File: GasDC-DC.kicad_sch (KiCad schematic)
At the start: 18 parts, among them IC1 TPS56637RPAR, J1 Conn_01x02, Q1 2N7002_SOT-23-3

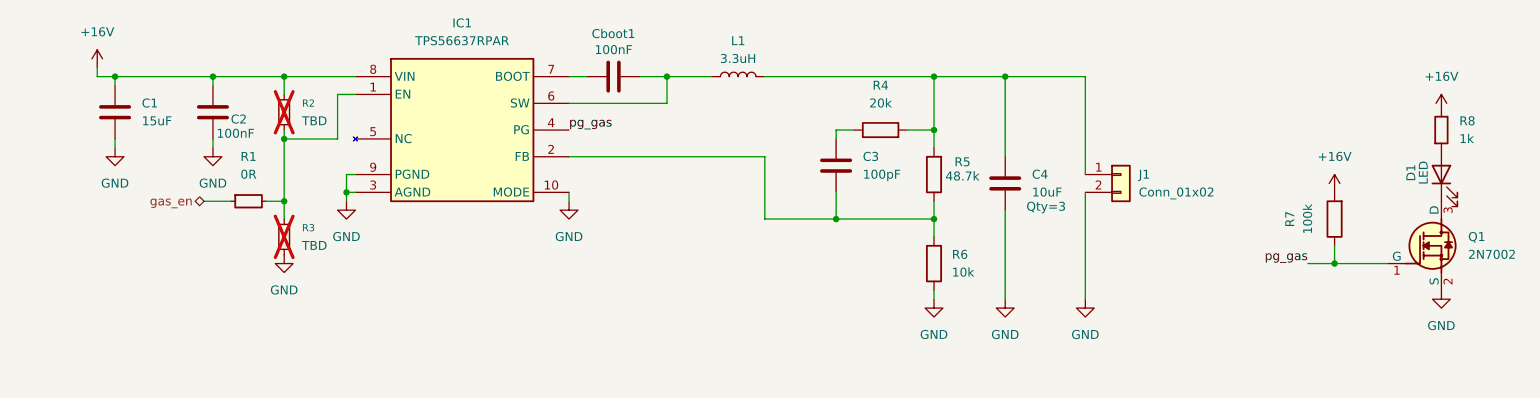
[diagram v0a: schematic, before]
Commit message: Minimal version without BMS
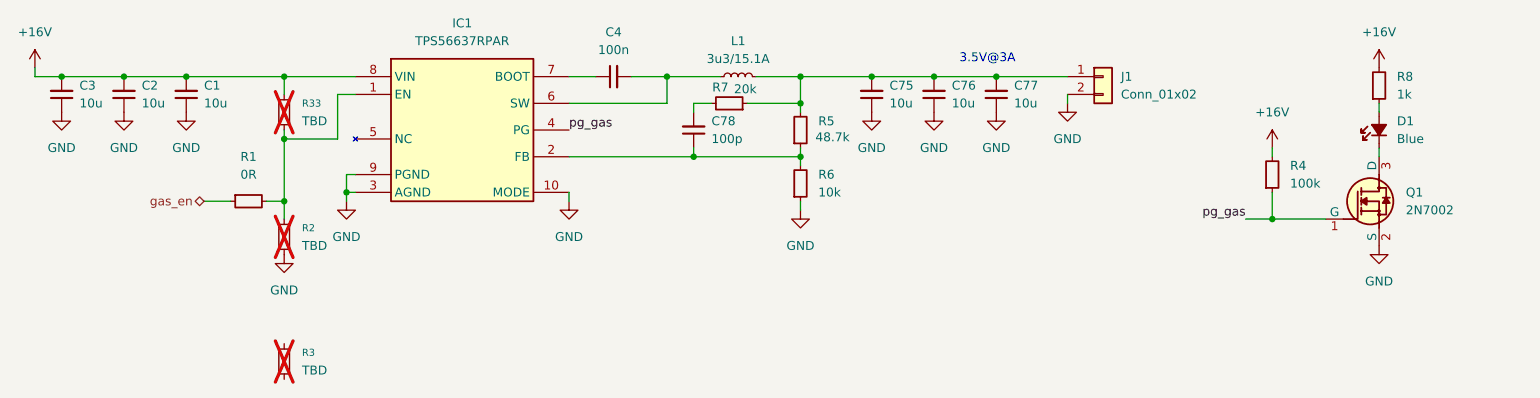
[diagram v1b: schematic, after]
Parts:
- removed C1: 15uF, symbol lib:C
- removed C2, Cboot1: 100nF, symbol lib:C
- removed C3: 100pF, symbol lib:C
- removed C4: 10uF, symbol lib:C
- removed D1: LED, symbol lib:LED
- removed L1: 3.3uH, symbol lib:L
- removed R4: 20k, symbol lib:R
- removed R5: 48.7k, symbol lib:R
- removed R6: 10k, symbol lib:R
- removed R7: 100k, symbol lib:R
- added C1, C2, C3, C75, C76, C77: C_10u_1206, Hardware Components Footprints:C_1206_3216Metric, symbol Hardware Components:C_10u_1206
- added C4: C_100n_16V_X7R_0402, Hardware Components Footprints:C_0402_1005Metric, symbol Hardware Components:C_100n_16V_X7R_0402
- added C78: C_100p_0402, Hardware Components Footprints:C_0402_1005Metric, symbol Hardware Components:C_100p_0402
- added D1: LED_B_0603_KP-1608QBC-D, Hardware Components Footprints:LED_0603_1608Metric_B, symbol Hardware Components:LED_B_0603_KP-1608QBC-D
- added L1: L_3u3_15.1A_Coilcraft-XAL7070, Hardware Components Footprints:L_Coilcraft-XAL7070, symbol Hardware Components:L_3u3_15.1A_Coilcraft-XAL7070
- added R33: TBD, Hardware Components Footprints:R_0402_1005Metric, symbol lib:R_Small
- added R4: R_100k_0402, Hardware Components Footprints:R_0402_1005Metric, symbol Hardware Components:R_100k_0402
- added R5: R_48k7_0402, Hardware Components Footprints:R_0402_1005Metric, symbol Hardware Components:R_4k7_0402
- added R6: R_10k_0402, Hardware Components Footprints:R_0402_1005Metric, symbol lib:R_10k_0402
- added R7: R_20k_0402, Hardware Components Footprints:R_0402_1005Metric, symbol Hardware Components:R_20k_0402
- J1: footprint (none) -> TerminalBlock_Phoenix:TerminalBlock_Phoenix_MKDS-1,5-2-5.08_1x02_P5.08mm_Horizontal
- R2, R3: footprint (none) -> Hardware Components Footprints:R_0402_1005Metric
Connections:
- net +16V: now also C1.2, C2.2, C3.2, R33.1, R4.2; no longer R2.1
- net GND: now also R2.2, C1.1, C2.1, C3.1, C75.1, C76.1, C77.1, R6.1; no longer R3.2
- net pg_gas: now also R4.1
- net at IC1.7 (BOOT): now also C4.1
- net at IC1.6 (SW): now also C4.2, L1.1
- net at Q1.3 (D): now also D1.1 (C)
- net at R8.1: now also D1.2 (A)
- net at IC1.2 (FB): now also C78.1, R5.1, R6.2
- net at J1.1 (Pin_1): now also C75.2, C76.2, C77.2, L1.2, R5.2, R7.1
- net at IC1.1 (EN), R1.2: now also R2.1, R33.2; no longer R2.2, R3.1
- new net: C78.2, R7.2
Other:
- note added: "3.5V@3A"
- moved on the sheet: J1, Q1, R2, R3, R8
